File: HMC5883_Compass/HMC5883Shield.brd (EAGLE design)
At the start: 39.5 x 26.7 mm, 7 parts

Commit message: Updated stencil text Added PCA9685 and ITG3200 shields
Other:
- board text added: "Nerduino HMC5883 Shield I2C 0x?? www.nerduino.com"
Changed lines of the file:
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@@
 <wire x1="40.056" y1="27.041" x2="0.508" y2="27.168" width="0" layer="20"/>
 <wire x1="0.508" y1="27.168" x2="0.508" y2="0.635" width="0" layer="20"/>
+<text x="10.414" y="5.461" size="1.778" layer="121">Nerduino
+HMC5883 Shield
+I2C 0x??
+www.nerduino.com</text>
 </plain>
 <attributes>
@@
 </board>
 </drawing>
+<compatibility>
+<note version="6.3" minversion="6.2.2" severity="warning">
+Since Version 6.2.2 text objects can contain more than one line,
+which will not be processed correctly with this version.
+</note>
+</compatibility>
 </eagle>

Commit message: Added solder jumpers for address and added resistors to output pins on pca9685 shield Updated labels
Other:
- board text added: "Nerduino HMC5883 Shield I2C 0x1E www.nerduino.com"
- board text removed: "Nerduino HMC5883 Shield I2C 0x?? www.nerduino.com"
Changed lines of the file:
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@@
 <text x="10.414" y="5.461" size="1.778" layer="121">Nerduino
 HMC5883 Shield
-I2C 0x??
+I2C 0x1E
 www.nerduino.com</text>
 </plain>

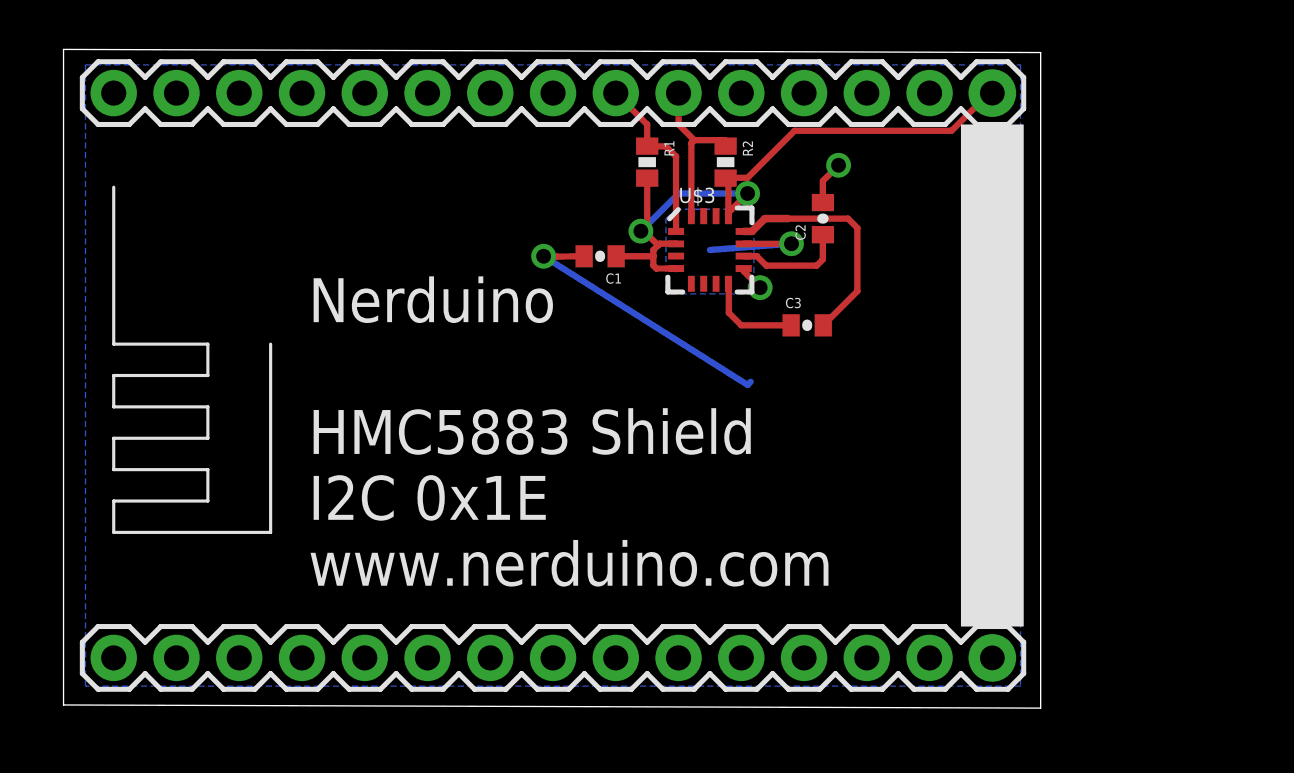
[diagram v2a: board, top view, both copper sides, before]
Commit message: Added OLED Shield Added LiPo Battery Charger Shield Updated outlines of all shields to match the cutout of the nodemcu board
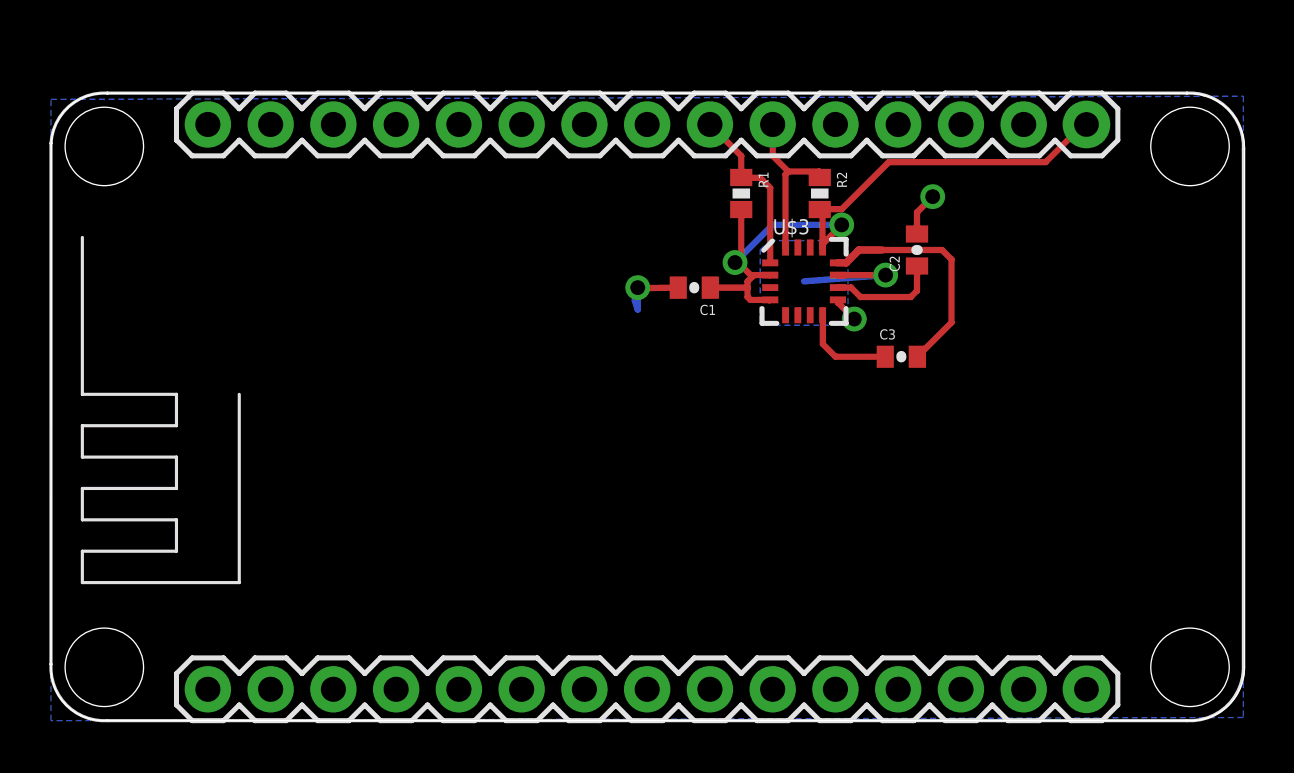
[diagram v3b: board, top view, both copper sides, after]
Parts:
- moved R1 4.02 mm to (27.9, 21.3)
- moved C3 4.02 mm to (34.4, 14.7)
- moved R2 4.02 mm to (31.1, 21.3)
- moved C1 4.02 mm to (26.0, 17.5)
- moved C2 4.02 mm to (35.1, 19.1)
- moved U$1 4.02 mm to (24.1, 6.35)
- moved U$3 4.02 mm to (30.5, 17.8)
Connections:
- net GND: now also U$1.10, U$1.17, U$1.24
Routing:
- net GND: track 20.3 -> 11.6 mm
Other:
- board size 39.5 x 26.7 mm -> 48.3 x 25.4 mm

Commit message: Updated the i2c pins to all shields to use d11/d12  as these pins will have dual use with the upcoming wifimcu Added FM24W256  Fram shield Added X95840 Digital potentiometer Shield Added AD5696 DAC Shield
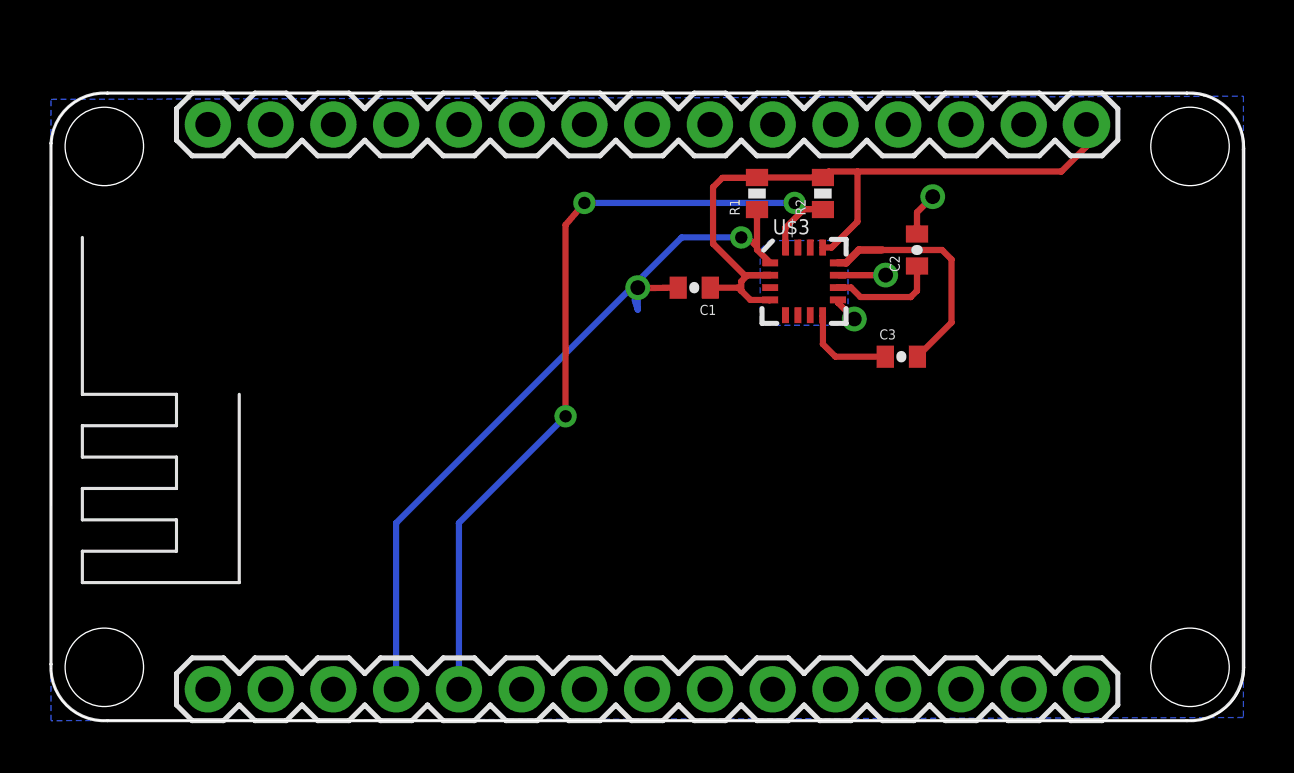
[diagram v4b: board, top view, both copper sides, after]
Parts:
- moved R1 0.63 mm to (28.6, 21.3), turned to 90 degrees
- moved R2 0.13 mm to (31.2, 21.3), turned to 90 degrees
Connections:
- net GND: no longer U$1.24
- net N$2: now also U$1.5; no longer U$1.21
- net N$3: now also U$1.4; no longer U$1.22
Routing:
- net N$2: track 6.79 -> 33.4 mm, vias 0 -> 3
- net N$3: track 7.05 -> 28.7 mm, vias 0 -> 1
- net GND: track 11.6 -> 8.49 mm
- net 3.3V: track 27.3 -> 30.0 mm, vias 2 -> 0
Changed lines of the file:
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@@
 <element name="C2" library="SparkFun" package="0402-CAP" value="4.7uF" x="35.052" y="19.05" rot="R90"/>
 <element name="C3" library="SparkFun" package="0402-CAP" value="0.22uF" x="34.417" y="14.732"/>
-<element name="R1" library="SparkFun" package="0402-RES" value="4.7k" x="27.94" y="21.336" rot="R270"/>
-<element name="R2" library="SparkFun" package="0402-RES" value="4.7k" x="31.115" y="21.336" rot="R270"/>
+<element name="R1" library="SparkFun" package="0402-RES" value="4.7k" x="28.575" y="21.336" rot="R90"/>
+<element name="R2" library="SparkFun" package="0402-RES" value="4.7k" x="31.242" y="21.336" rot="R90"/>
 <element name="U$1" library="NerduinoShieldLib" package="NERDUINO_STACK" value="NERDSHIELD" x="24.13" y="6.35"/>
 <element name="U$3" library="SparkFun" package="16LPCC" value="HMC5883LSMD" x="30.48" y="17.78"/>
@@
 <wire x1="33.651" y1="18.03" x2="33.782" y2="18.034" width="0.254" layer="1"/>
 <via x="33.782" y="18.034" extent="1-16" drill="0.6" shape="square"/>
-<wire x1="33.782" y1="18.034" x2="30.48" y2="17.78" width="0.254" layer="16"/>
+<wire x1="33.782" y1="18.034" x2="33.655" y2="18.161" width="0.254" layer="16"/>
 <wire x1="25.385" y1="17.526" x2="24.272" y2="17.511" width="0.254" layer="1"/>
 <wire x1="24.272" y1="17.511" x2="23.749" y2="17.526" width="0.254" layer="1"/>
@@
 <contactref element="U$1" pad="10"/>
 <contactref element="U$1" pad="17"/>
-<contactref element="U$1" pad="24"/>
 </signal>
 <signal name="3.3V">
@@
 <contactref element="R1" pad="2"/>
 <wire x1="29.083" y1="17.003" x2="29.11" y2="17.03" width="0.254" layer="1"/>
+<wire x1="41.91" y1="24.13" x2="41.91" y2="23.241" width="0.254" layer="1"/>
+<wire x1="41.91" y1="23.241" x2="40.894" y2="22.225" width="0.254" layer="1"/>
+<wire x1="40.894" y1="22.225" x2="32.639" y2="22.225" width="0.254" layer="1"/>
+<wire x1="32.639" y1="22.225" x2="31.481" y2="22.225" width="0.254" layer="1"/>
+<wire x1="31.481" y1="22.225" x2="31.242" y2="21.986" width="0.254" layer="1"/>
+<wire x1="31.242" y1="21.986" x2="28.575" y2="21.986" width="0.254" layer="1"/>
+<wire x1="31.23" y1="19.15" x2="31.596" y2="19.15" width="0.254" layer="1"/>
+<wire x1="31.596" y1="19.15" x2="32.639" y2="20.193" width="0.254" layer="1"/>
+<wire x1="32.639" y1="20.193" x2="32.639" y2="22.225" width="0.254" layer="1"/>
 <wire x1="29.11" y1="17.03" x2="28.309" y2="17.03" width="0.254" layer="1"/>
-<wire x1="28.309" y1="17.03" x2="28.194" y2="17.145" width="0.254" layer="1"/>
-<wire x1="28.194" y1="17.145" x2="28.194" y2="17.526" width="0.254" layer="1"/>
-<wire x1="28.194" y1="17.526" x2="28.194" y2="17.78" width="0.254" layer="1"/>
-<wire x1="28.194" y1="17.78" x2="28.3845" y2="17.9705" width="0.254" layer="1"/>
-<wire x1="28.3845" y1="17.9705" x2="28.448" y2="18.034" width="0.254" layer="1"/>
-<wire x1="28.448" y1="18.034" x2="29.106" y2="18.034" width="0.254" layer="1"/>
+<wire x1="28.309" y1="17.03" x2="27.94" y2="17.399" width="0.254" layer="1"/>
+<wire x1="27.94" y1="17.399" x2="27.94" y2="17.78" width="0.254" layer="1"/>
+<wire x1="27.94" y1="17.78" x2="28.194" y2="18.034" width="0.254" layer="1"/>
+<wire x1="28.194" y1="18.034" x2="29.106" y2="18.034" width="0.254" layer="1"/>
 <wire x1="29.106" y1="18.034" x2="29.11" y2="18.03" width="0.254" layer="1"/>
-<wire x1="26.685" y1="17.526" x2="28.194" y2="17.526" width="0.254" layer="1"/>
-<wire x1="31.23" y1="19.15" x2="31.23" y2="20.571" width="0.254" layer="1"/>
-<wire x1="31.23" y1="20.571" x2="31.115" y2="20.686" width="0.254" layer="1"/>
-<wire x1="41.91" y1="24.13" x2="41.783" y2="24.13" width="0.254" layer="1"/>
-<wire x1="41.783" y1="24.13" x2="40.259" y2="22.606" width="0.254" layer="1"/>
-<wire x1="40.259" y1="22.606" x2="33.909" y2="22.606" width="0.254" layer="1"/>
-<wire x1="33.909" y1="22.606" x2="32.004" y2="20.701" width="0.254" layer="1"/>
-<wire x1="32.004" y1="20.701" x2="31.13" y2="20.701" width="0.254" layer="1"/>
-<wire x1="31.13" y1="20.701" x2="31.115" y2="20.686" width="0.254" layer="1"/>
-<wire x1="27.94" y1="20.686" x2="27.94" y2="18.542" width="0.254" layer="1"/>
-<wire x1="27.94" y1="18.542" x2="27.94" y2="18.415" width="0.254" layer="1"/>
-<wire x1="27.94" y1="18.415" x2="28.3845" y2="17.9705" width="0.254" layer="1"/>
-<wire x1="31.23" y1="19.15" x2="31.23" y2="19.292" width="0.254" layer="1"/>
-<wire x1="31.23" y1="19.292" x2="32.004" y2="20.066" width="0.254" layer="1"/>
-<via x="32.004" y="20.066" extent="1-16" drill="0.6"/>
-<wire x1="32.004" y1="20.066" x2="29.21" y2="20.066" width="0.254" layer="16"/>
-<wire x1="29.21" y1="20.066" x2="27.686" y2="18.542" width="0.254" layer="16"/>
-<via x="27.686" y="18.542" extent="1-16" drill="0.6"/>
-<wire x1="27.686" y1="18.542" x2="27.94" y2="18.542" width="0.254" layer="1"/>
+<wire x1="26.685" y1="17.526" x2="27.813" y2="17.526" width="0.254" layer="1"/>
+<wire x1="27.813" y1="17.526" x2="27.94" y2="17.399" width="0.254" layer="1"/>
+<wire x1="29.11" y1="18.03" x2="28.071" y2="18.03" width="0.254" layer="1"/>
+<wire x1="28.071" y1="18.03" x2="26.797" y2="19.304" width="0.254" layer="1"/>
+<wire x1="26.797" y1="19.304" x2="26.797" y2="21.59" width="0.254" layer="1"/>
+<wire x1="26.797" y1="21.59" x2="27.178" y2="21.971" width="0.254" layer="1"/>
+<wire x1="27.178" y1="21.971" x2="28.56" y2="21.971" width="0.254" layer="1"/>
+<wire x1="28.56" y1="21.971" x2="28.575" y2="21.986" width="0.254" layer="1"/>
 </signal>
 <signal name="N$2">
 <contactref element="R2" pad="1"/>
-<contactref element="U$1" pad="21"/>
 <contactref element="U$3" pad="16"/>
-<wire x1="29.21" y1="24.13" x2="29.21" y2="22.86" width="0.254" layer="1"/>
-<wire x1="29.21" y1="22.86" x2="29.845" y2="22.225" width="0.254" layer="1"/>
-<wire x1="29.845" y1="22.225" x2="31.1" y2="22.225" width="0.254" layer="1"/>
-<wire x1="31.1" y1="22.225" x2="31.115" y2="21.986" width="0.254" layer="1"/>
-<wire x1="29.73" y1="19.15" x2="29.73" y2="22.11" width="0.254" layer="1"/>
-<wire x1="29.73" y1="22.11" x2="29.845" y2="22.225" width="0.254" layer="1"/>
+<contactref element="U$1" pad="5"/>
+<wire x1="31.242" y1="20.686" x2="31.242" y2="20.701" width="0.254" layer="1"/>
+<wire x1="31.242" y1="20.701" x2="30.48" y2="20.701" width="0.254" layer="1"/>
+<wire x1="30.48" y1="20.701" x2="29.718" y2="19.939" width="0.254" layer="1"/>
+<wire x1="29.718" y1="19.939" x2="29.718" y2="19.162" width="0.254" layer="1"/>
+<wire x1="29.718" y1="19.162" x2="29.73" y2="19.15" width="0.254" layer="1"/>
+<wire x1="16.51" y1="1.27" x2="16.51" y2="8.001" width="0.254" layer="16"/>
+<wire x1="16.51" y1="8.001" x2="20.828" y2="12.319" width="0.254" layer="16"/>
+<via x="20.828" y="12.319" extent="1-16" drill="0.5"/>
+<wire x1="20.828" y1="12.319" x2="20.828" y2="20.066" width="0.254" layer="1"/>
+<wire x1="20.828" y1="20.066" x2="21.59" y2="20.955" width="0.254" layer="1"/>
+<via x="21.59" y="20.955" extent="1-16" drill="0.5"/>
+<wire x1="21.59" y1="20.955" x2="30.099" y2="20.955" width="0.254" layer="16"/>
+<via x="30.099" y="20.955" extent="1-16" drill="0.5"/>
+<wire x1="30.099" y1="20.955" x2="30.353" y2="20.828" width="0.254" layer="1"/>
+<wire x1="30.353" y1="20.828" x2="30.48" y2="20.701" width="0.254" layer="1"/>
 </signal>
 <signal name="N$3">
 <contactref element="R1" pad="1"/>
-<contactref element="U$1" pad="22"/>
 <contactref element="U$3" pad="1"/>
-<wire x1="29.11" y1="18.53" x2="29.11" y2="21.563" width="0.254" layer="1"/>
-<wire x1="29.11" y1="21.563" x2="28.702" y2="21.971" width="0.254" layer="1"/>
-<wire x1="28.702" y1="21.971" x2="27.955" y2="21.971" width="0.254" layer="1"/>
-<wire x1="27.955" y1="21.971" x2="27.94" y2="21.986" width="0.254" layer="1"/>
-<wire x1="27.94" y1="21.986" x2="27.94" y2="22.86" width="0.254" layer="1"/>
-<wire x1="27.94" y1="22.86" x2="26.67" y2="24.13" width="0.254" layer="1"/>
+<contactref element="U$1" pad="4"/>
+<wire x1="28.575" y1="20.686" x2="28.575" y2="19.177" width="0.254" layer="1"/>
+<wire x1="28.575" y1="19.177" x2="28.575" y2="19.065" width="0.254" layer="1"/>
+<wire x1="28.575" y1="19.065" x2="29.11" y2="18.53" width="0.254" layer="1"/>
+<wire x1="13.97" y1="1.27" x2="13.97" y2="8.001" width="0.254" layer="16"/>
+<wire x1="13.97" y1="8.001" x2="25.527" y2="19.558" width="0.254" layer="16"/>
+<wire x1="25.527" y1="19.558" x2="27.94" y2="19.558" width="0.254" layer="16"/>
+<via x="27.94" y="19.558" extent="1-16" drill="0.5"/>
+<wire x1="27.94" y1="19.558" x2="28.194" y2="19.558" width="0.254" layer="1"/>
+<wire x1="28.194" y1="19.558" x2="28.575" y2="19.177" width="0.254" layer="1"/>
 </signal>
 <signal name="N$1">
